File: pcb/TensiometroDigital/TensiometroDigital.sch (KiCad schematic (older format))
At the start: 14 parts

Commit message: cambios al sch
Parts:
- removed BZ?: Buzzer, symbol Device:Buzzer
- removed C? (x2): CP1, symbol Device:CP1
- removed D?: LED, symbol Device:LED
- removed R? (x6): R, symbol Device:R
- removed U?: LPC1769FBD100, Package_QFP:LQFP-100_14x14mm_P0.5mm, symbol MCU_NXP_LPC:LPC1769FBD100
- removed U?: MPX5050GP, symbol TensiometroDigital:MPX5050GP
- removed U? (x2): LM324, symbol Amplifier_Operational:LM324
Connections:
- net labels removed: +5V, GND
- wire segments 25 -> 11
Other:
- note removed: "#DUDA. Esta bien colocar los pines de alimentacion de 324 asi no más? Problemas con DRC ?"
- note removed: "#DUDAD CON MODELO. MODELO NO COINCIDE CON PINOUT DATASHEET\n\n"
- note removed: "#cambiar el LCD"
- note removed: "¿A qué pines conectar cada cosa?"

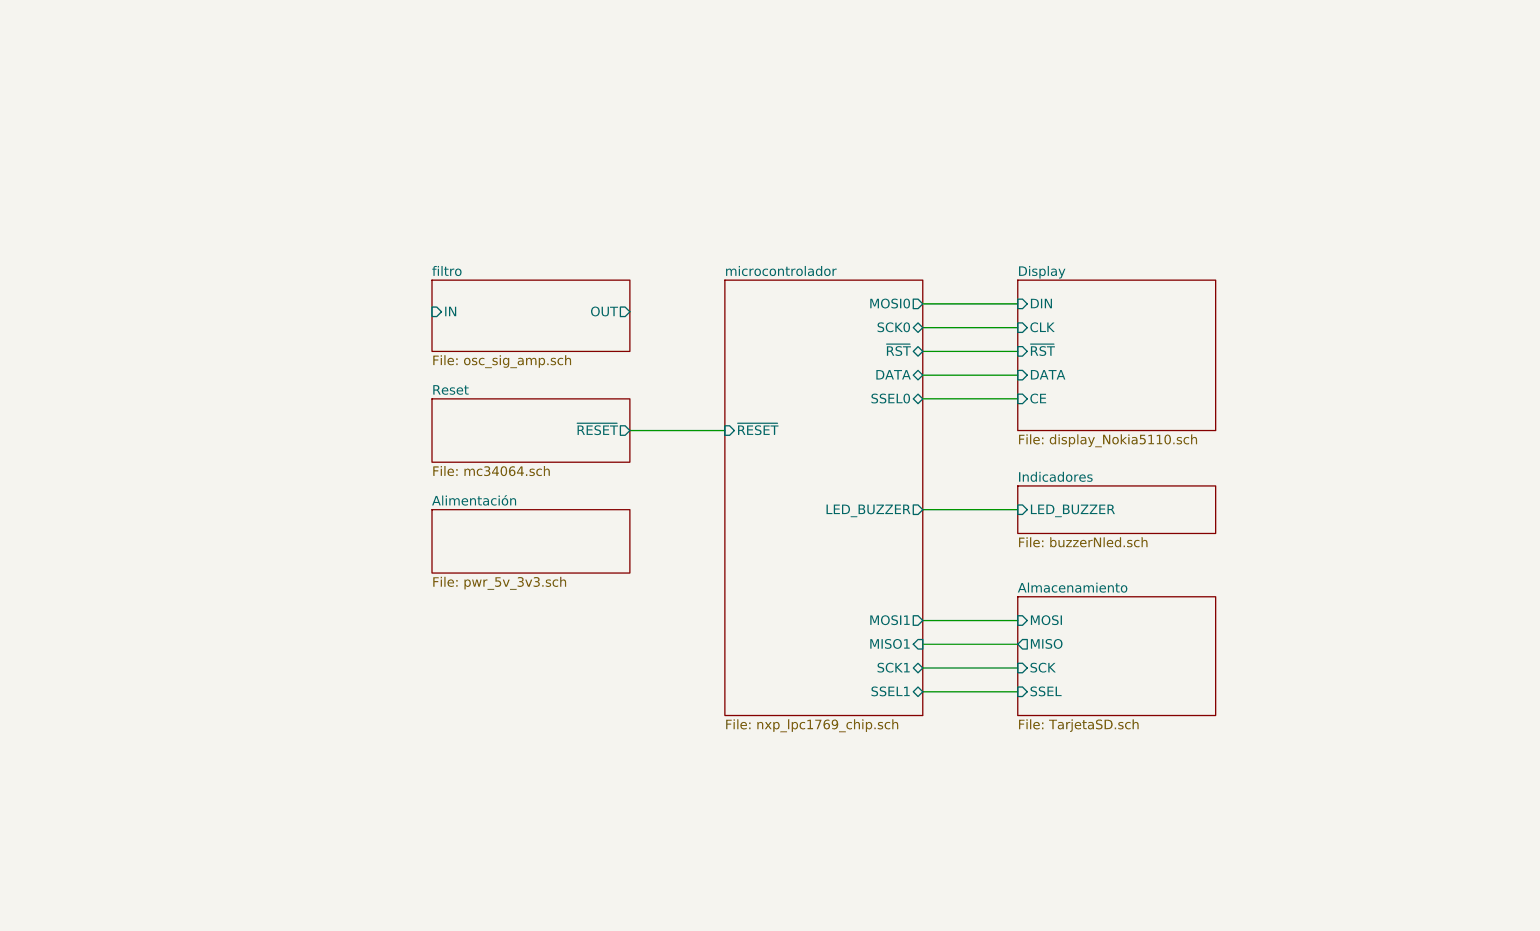
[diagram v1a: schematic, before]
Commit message: Finalizado: SCH, PCB, GABINETE, DRAWINGS. FALTA: GERBERS, BOM e Informe
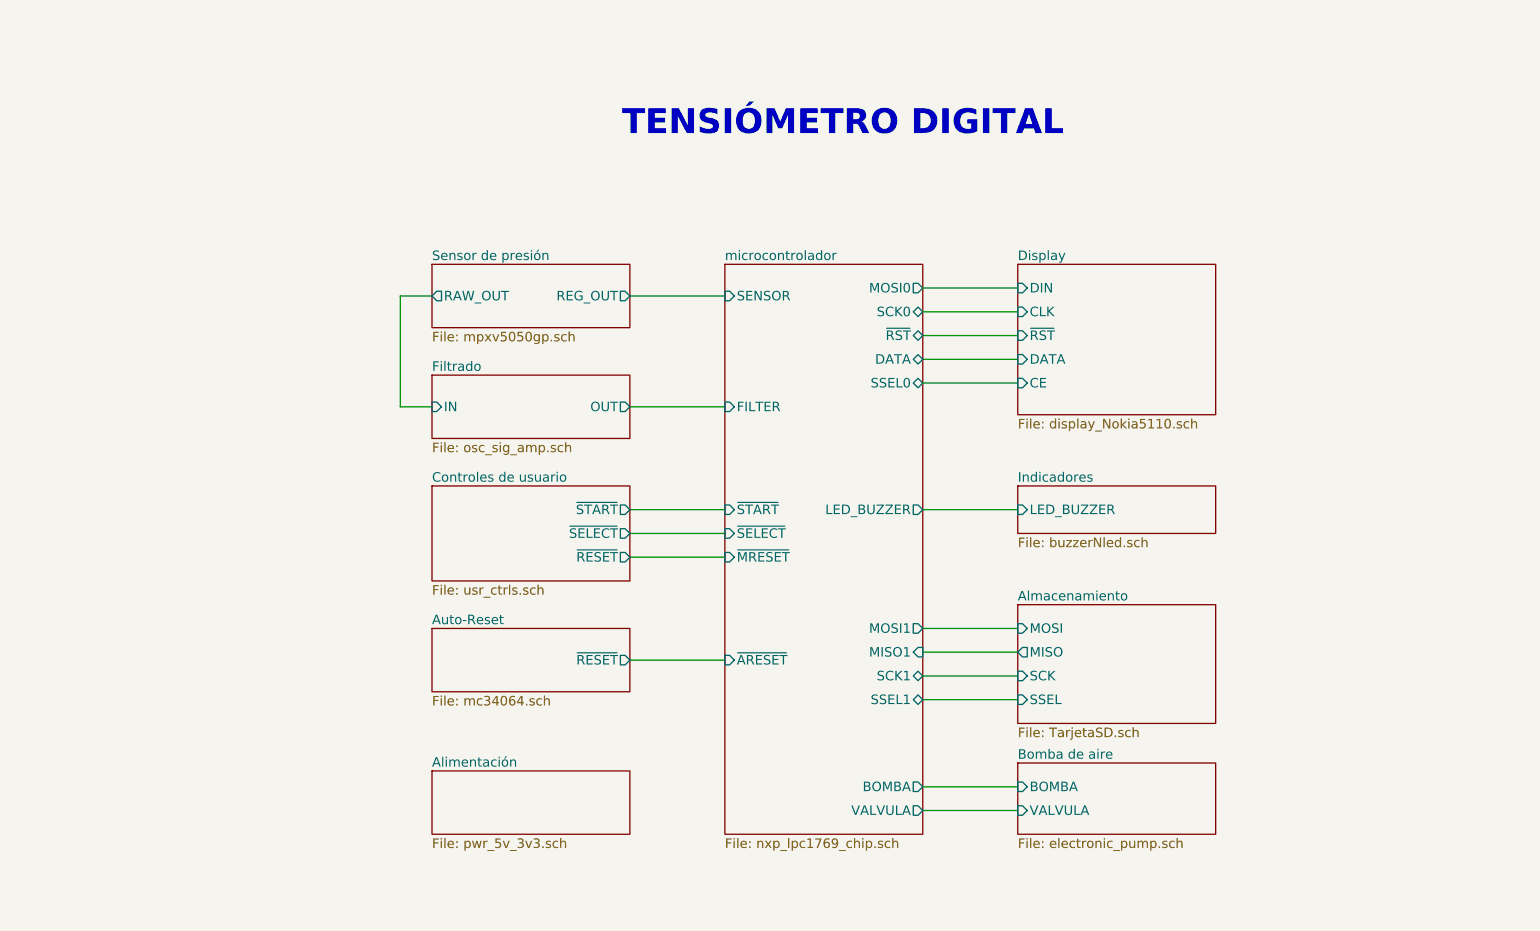
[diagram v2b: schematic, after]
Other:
- note added: "TENSIÓMETRO DIGITAL"
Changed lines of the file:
@@
 LIBS:lm2940
 LIBS:lm2575
+LIBS:bav199
+LIBS:mpxv5050gp
+LIBS:lm8364
 LIBS:TensiometroDigital-cache
 EELAYER 25 0
@@
 $Descr A4 11693 8268
 encoding utf-8
-Sheet 1 8
-Title ""
-Date ""
-Rev ""
-Comp ""
-Comment1 ""
-Comment2 ""
-Comment3 ""
-Comment4 ""
+Sheet 1 11
+Title "TENSIÓMETRO DIGITAL"
+Date "2018-11-20"
+Rev "A"
+Comp "UTN - FRBA"
+Comment1 "Curso: R1032"
+Comment2 "Leg.: 153204-2"
+Comment3 "Autor: Alegre Mendoza Ezequiel"
+Comment4 "SDR Proyecto Final"
 $EndDescr
 $Sheet
-S 3400 2350 1250 450
-U 5BBD6290
-F0 "filtro" 60
-F1 "osc_sig_amp.sch" 60
-F2 "IN" I L 3400 2550 60
-F3 "OUT" O R 4650 2550 60
-$EndSheet
-$Sheet
-S 7100 2350 1250 950
+S 7100 2250 1250 950
 U 5BBD63C0
 F0 "Display" 60
 F1 "display_Nokia5110.sch" 60
-F2 "DIN" I L 7100 2500 60
-F3 "CLK" I L 7100 2650 60
-F4 "~RST" I L 7100 2800 60
-F5 "DATA" I L 7100 2950 60
-F6 "CE" I L 7100 3100 60
+F2 "DIN" I L 7100 2400 60
+F3 "CLK" I L 7100 2550 60
+F4 "~RST" I L 7100 2700 60
+F5 "DATA" I L 7100 2850 60
+F6 "CE" I L 7100 3000 60
 $EndSheet
 $Sheet
@@
 $EndSheet
 $Sheet
-S 3400 3100 1250 400
+S 3400 4550 1250 400
 U 5BBD647E
-F0 "Reset" 60
+F0 "Auto-Reset" 60
 F1 "mc34064.sch" 60
-F2 "~RESET" O R 4650 3300 60
+F2 "~RESET" O R 4650 4750 60
 $EndSheet
 $Sheet
-S 7100 4350 1250 750
+S 7100 4400 1250 750
 U 5BBF9B77
 F0 "Almacenamiento" 60
 F1 "TarjetaSD.sch" 60
-F2 "SSEL" I L 7100 4950 60
-F3 "MOSI" I L 7100 4500 60
-F4 "MISO" O L 7100 4650 60
-F5 "SCK" I L 7100 4800 60
+F2 "SSEL" I L 7100 5000 60
+F3 "MOSI" I L 7100 4550 60
+F4 "MISO" O L 7100 4700 60
+F5 "SCK" I L 7100 4850 60
 $EndSheet
 $Sheet
-S 3400 3800 1250 400
+S 3400 5450 1250 400
 U 5BBF9C03
 F0 "Alimentación" 60
 F1 "pwr_5v_3v3.sch" 60
 $EndSheet
-Wire Wire Line
-	6500 4500 7100 4500
-Wire Wire Line
-	6500 4650 7100 4650
-Wire Wire Line
-	7100 4800 6500 4800
-Wire Wire Line
-	6500 4950 7100 4950
-Wire Wire Line
-	6500 2500 7100 2500
-Wire Wire Line
-	6500 2650 7100 2650
-Wire Wire Line
-	6500 3100 7100 3100
 $Sheet
-S 5250 2350 1250 2750
+S 5250 2250 1250 3600
 U 5BBD623A
 F0 "microcontrolador" 60
 F1 "nxp_lpc1769_chip.sch" 60
-F2 "~RESET" I L 5250 3300 60
-F3 "MOSI1" O R 6500 4500 60
-F4 "MISO1" I R 6500 4650 60
-F5 "SCK1" B R 6500 4800 60
-F6 "SSEL1" B R 6500 4950 60
-F7 "SCK0" B R 6500 2650 60
-F8 "SSEL0" B R 6500 3100 60
-F9 "MOSI0" O R 6500 2500 60
-F10 "DATA" B R 6500 2950 60
-F11 "~RST" B R 6500 2800 60
-F12 "LED_BUZZER" O R 6500 3800 60
+F2 "MOSI1" O R 6500 4550 60
+F3 "MISO1" I R 6500 4700 60
+F4 "SCK1" B R 6500 4850 60
+F5 "SSEL1" B R 6500 5000 60
+F6 "SCK0" B R 6500 2550 60
+F7 "SSEL0" B R 6500 3000 60
+F8 "MOSI0" O R 6500 2400 60
+F9 "DATA" B R 6500 2850 60
+F10 "~RST" B R 6500 2700 60
+F11 "LED_BUZZER" O R 6500 3800 60
+F12 "SENSOR" I L 5250 2450 60
+F13 "~START" I L 5250 3800 60
+F14 "~SELECT" I L 5250 3950 60
+F15 "FILTER" I L 5250 3150 60
+F16 "~MRESET" I L 5250 4100 60
+F17 "~ARESET" I L 5250 4750 60
+F18 "BOMBA" O R 6500 5550 60
+F19 "VALVULA" O R 6500 5700 60
+$EndSheet
+$Sheet
+S 3400 2250 1250 400
+U 5BDB5C2D
+F0 "Sensor de presión" 60
+F1 "mpxv5050gp.sch" 60
+F2 "REG_OUT" O R 4650 2450 60
+F3 "RAW_OUT" O L 3400 2450 60
 $EndSheet
 Wire Wire Line
-	6500 2800 7100 2800
+	6500 2400 7100 2400
 Wire Wire Line
-	6500 2950 7100 2950
+	6500 2550 7100 2550
+Wire Wire Line
+	6500 3000 7100 3000
+Wire Wire Line
+	6500 2700 7100 2700
+Wire Wire Line
+	6500 2850 7100 2850
+Wire Wire Line
+	4650 2450 5250 2450
+Wire Wire Line
+	3200 2450 3200 3150
+Wire Wire Line
+	3200 3150 3400 3150
+Wire Wire Line
+	4650 3150 5250 3150
+$Sheet
+S 3400 3650 1250 600
+U 5BDE7733
+F0 "Controles de usuario" 60
+F1 "usr_ctrls.sch" 60
+F2 "~RESET" O R 4650 4100 60
+F3 "~START" O R 4650 3800 60
+F4 "~SELECT" O R 4650 3950 60
+$EndSheet
+Wire Wire Line
+	4650 4100 5250 4100
+Wire Wire Line
+	4650 3950 5250 3950
+Wire Wire Line
+	4650 3800 5250 3800
+Wire Wire Line
+	4650 4750 5250 4750
+$Sheet
+S 3400 2950 1250 400
+U 5BBD6290
+F0 "Filtrado" 60
+F1 "osc_sig_amp.sch" 60
+F2 "OUT" O R 4650 3150 60
+F3 "IN" I L 3400 3150 60
+$EndSheet
+Wire Wire Line
+	3400 2450 3200 2450
+$Sheet
+S 7100 5400 1250 450
+U 5BE17B11
+F0 "Bomba de aire" 60
+F1 "electronic_pump.sch" 60
+F2 "BOMBA" I L 7100 5550 60
+F3 "VALVULA" I L 7100 5700 60
+$EndSheet
+Wire Wire Line
+	6500 4550 7100 4550
+Wire Wire Line
+	6500 4700 7100 4700
+Wire Wire Line
+	7100 4850 6500 4850
+Wire Wire Line
+	6500 5000 7100 5000
+Wire Wire Line
+	6500 5550 7100 5550
+Wire Wire Line
+	7100 5700 6500 5700
 Wire Wire Line
 	6500 3800 7100 3800
-Wire Wire Line
-	4650 3300 5250 3300
+Text Notes 4600 1450 0    157  ~ 31
+TENSIÓMETRO DIGITAL
 $EndSCHEMATC
